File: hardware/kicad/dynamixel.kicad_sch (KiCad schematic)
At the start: 0 parts

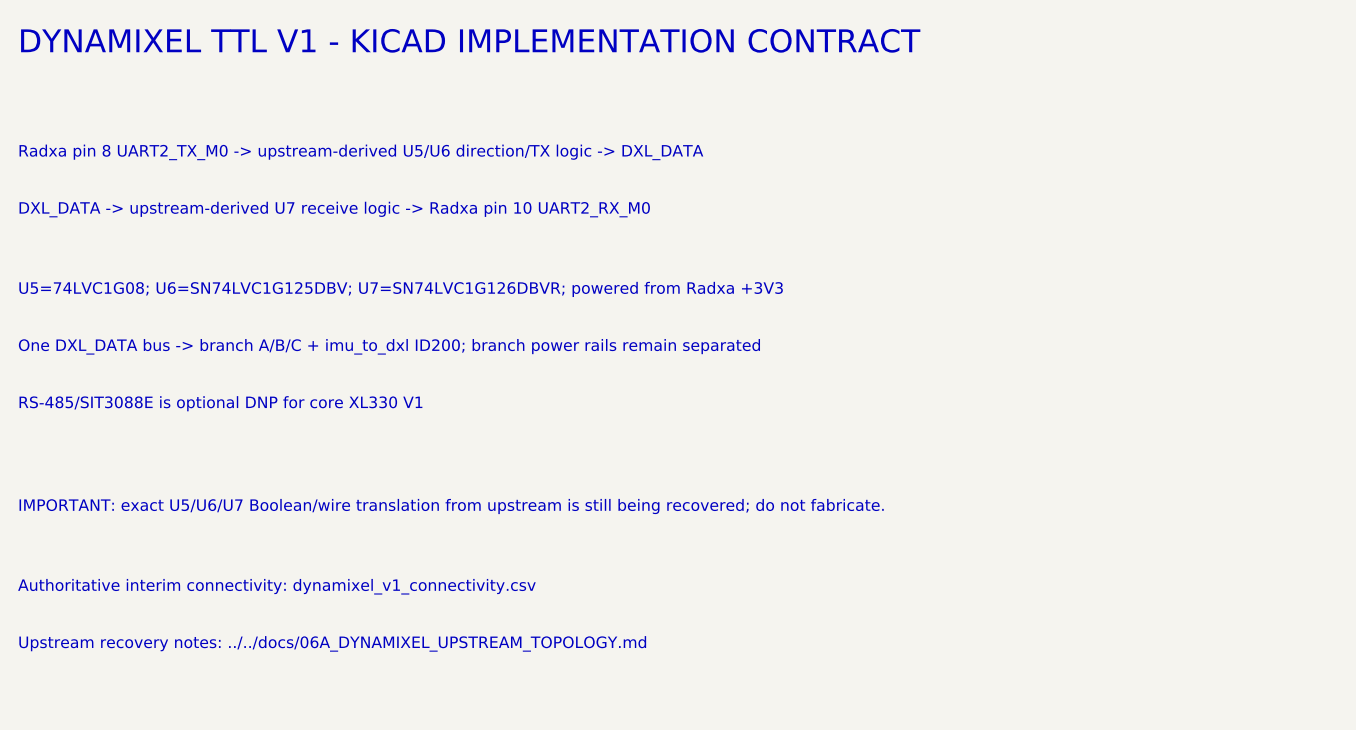
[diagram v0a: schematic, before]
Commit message: correct Dynamixel schematic contract TX RX roles
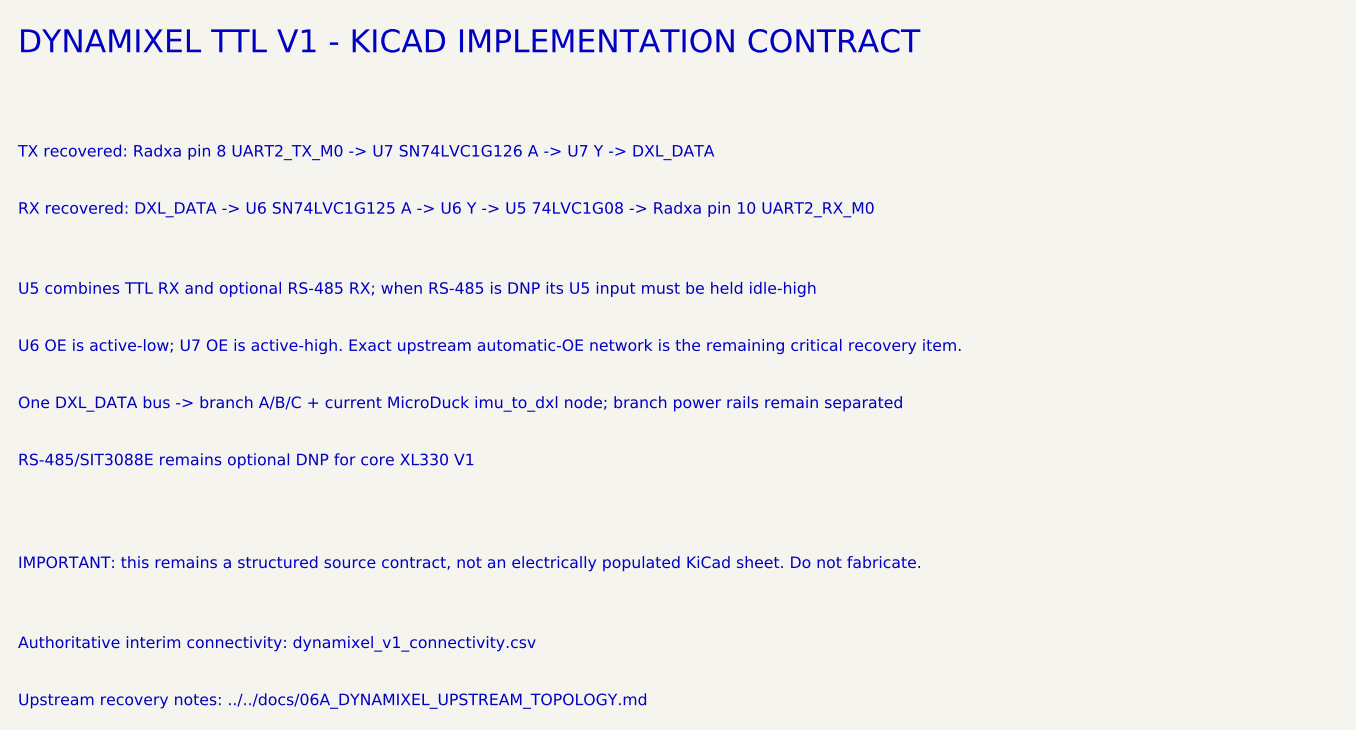
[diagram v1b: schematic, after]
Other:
- note added: "IMPORTANT: this remains a structured source contract, not an electrically populated KiCad sheet. Do not fabricate."
- note added: "One DXL_DATA bus -> branch A/B/C + current MicroDuck imu_to_dxl node; branch power rails remain separated"
- note added: "RS-485/SIT3088E remains optional DNP for core XL330 V1"
- note added: "RX recovered: DXL_DATA -> U6 SN74LVC1G125 A -> U6 Y -> U5 74LVC1G08 -> Radxa pin 10 UART2_RX_M0"
- note added: "TX recovered: Radxa pin 8 UART2_TX_M0 -> U7 SN74LVC1G126 A -> U7 Y -> DXL_DATA"
- note added: "U5 combines TTL RX and optional RS-485 RX; when RS-485 is DNP its U5 input must be held idle-high"
- note added: "U6 OE is active-low; U7 OE is active-high. Exact upstream automatic-OE network is the remaining critical recovery item."
- note removed: "DXL_DATA -> upstream-derived U7 receive logic -> Radxa pin 10 UART2_RX_M0"
- note removed: "IMPORTANT: exact U5/U6/U7 Boolean/wire translation from upstream is still being recovered; do not fabricate."
- note removed: "One DXL_DATA bus -> branch A/B/C + imu_to_dxl ID200; branch power rails remain separated"
- note removed: "RS-485/SIT3088E is optional DNP for core XL330 V1"
- note removed: "Radxa pin 8 UART2_TX_M0 -> upstream-derived U5/U6 direction/TX logic -> DXL_DATA"
- note removed: "U5=74LVC1G08; U6=SN74LVC1G125DBV; U7=SN74LVC1G126DBVR; powered from Radxa +3V3"
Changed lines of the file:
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@@
     (title "Radxa ZERO 3W Robot HAT - Dynamixel TTL V1")
     (date "2026-09-09")
-    (rev "v0.8-dev")
+    (rev "v0.9-dev")
     (company "juper007 / DIY")
     (comment 1 "DESIGN DRAFT - NOT FABRICATION READY")
@@
     (effects (font (size 2.54 2.54) (thickness 0.4)) (justify left bottom))
   )
-  (text "Radxa pin 8 UART2_TX_M0 -> upstream-derived U5/U6 direction/TX logic -> DXL_DATA"
+  (text "TX recovered: Radxa pin 8 UART2_TX_M0 -> U7 SN74LVC1G126 A -> U7 Y -> DXL_DATA"
     (exclude_from_sim no)
     (at 20.32 31.75 0)
     (effects (font (size 1.27 1.27)) (justify left bottom))
   )
-  (text "DXL_DATA -> upstream-derived U7 receive logic -> Radxa pin 10 UART2_RX_M0"
+  (text "RX recovered: DXL_DATA -> U6 SN74LVC1G125 A -> U6 Y -> U5 74LVC1G08 -> Radxa pin 10 UART2_RX_M0"
     (exclude_from_sim no)
     (at 20.32 38.1 0)
     (effects (font (size 1.27 1.27)) (justify left bottom))
   )
-  (text "U5=74LVC1G08; U6=SN74LVC1G125DBV; U7=SN74LVC1G126DBVR; powered from Radxa +3V3"
+  (text "U5 combines TTL RX and optional RS-485 RX; when RS-485 is DNP its U5 input must be held idle-high"
     (exclude_from_sim no)
     (at 20.32 47.0 0)
     (effects (font (size 1.27 1.27)) (justify left bottom))
   )
-  (text "One DXL_DATA bus -> branch A/B/C + imu_to_dxl ID200; branch power rails remain separated"
+  (text "U6 OE is active-low; U7 OE is active-high. Exact upstream automatic-OE network is the remaining critical recovery item."
     (exclude_from_sim no)
     (at 20.32 53.35 0)
     (effects (font (size 1.27 1.27)) (justify left bottom))
   )
-  (text "RS-485/SIT3088E is optional DNP for core XL330 V1"
+  (text "One DXL_DATA bus -> branch A/B/C + current MicroDuck imu_to_dxl node; branch power rails remain separated"
     (exclude_from_sim no)
     (at 20.32 59.7 0)
     (effects (font (size 1.27 1.27)) (justify left bottom))
   )
-  (text "IMPORTANT: exact U5/U6/U7 Boolean/wire translation from upstream is still being recovered; do not fabricate."
+  (text "RS-485/SIT3088E remains optional DNP for core XL330 V1"
     (exclude_from_sim no)
-    (at 20.32 71.12 0)
+    (at 20.32 66.05 0)
+    (effects (font (size 1.27 1.27)) (justify left bottom))
+  )
+  (text "IMPORTANT: this remains a structured source contract, not an electrically populated KiCad sheet. Do not fabricate."
+    (exclude_from_sim no)
+    (at 20.32 77.47 0)
     (effects (font (size 1.27 1.27) (thickness 0.25)) (justify left bottom))
   )
   (text "Authoritative interim connectivity: dynamixel_v1_connectivity.csv"
     (exclude_from_sim no)
-    (at 20.32 80.01 0)
+    (at 20.32 86.36 0)
     (effects (font (size 1.27 1.27)) (justify left bottom))
   )
   (text "Upstream recovery notes: ../../docs/06A_DYNAMIXEL_UPSTREAM_TOPOLOGY.md"
     (exclude_from_sim no)
-    (at 20.32 86.36 0)
+    (at 20.32 92.71 0)
     (effects (font (size 1.27 1.27)) (justify left bottom))
   )

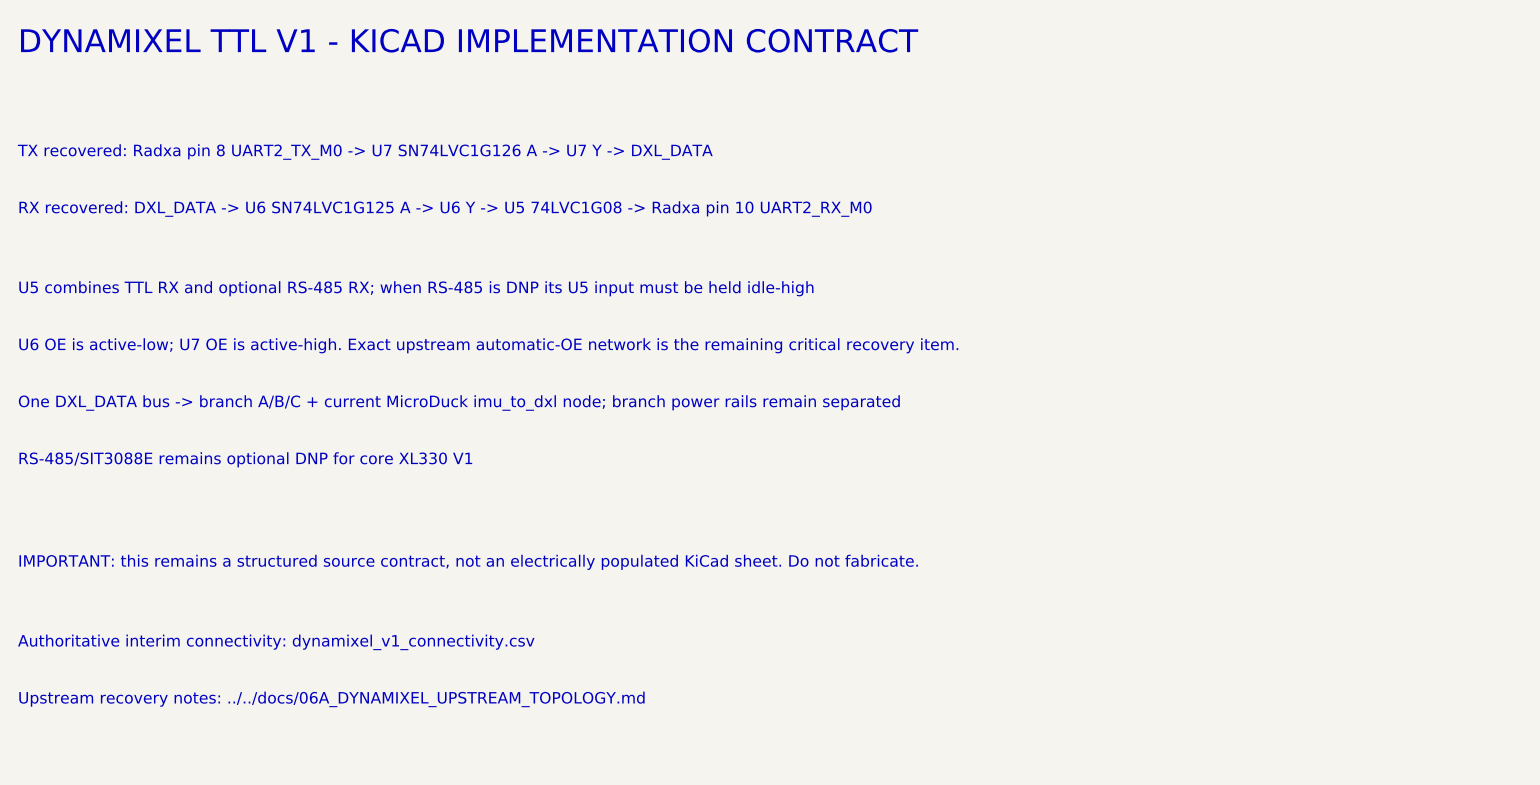
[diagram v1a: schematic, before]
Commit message: synchronize Dynamixel KiCad implementation contract with recovered topology
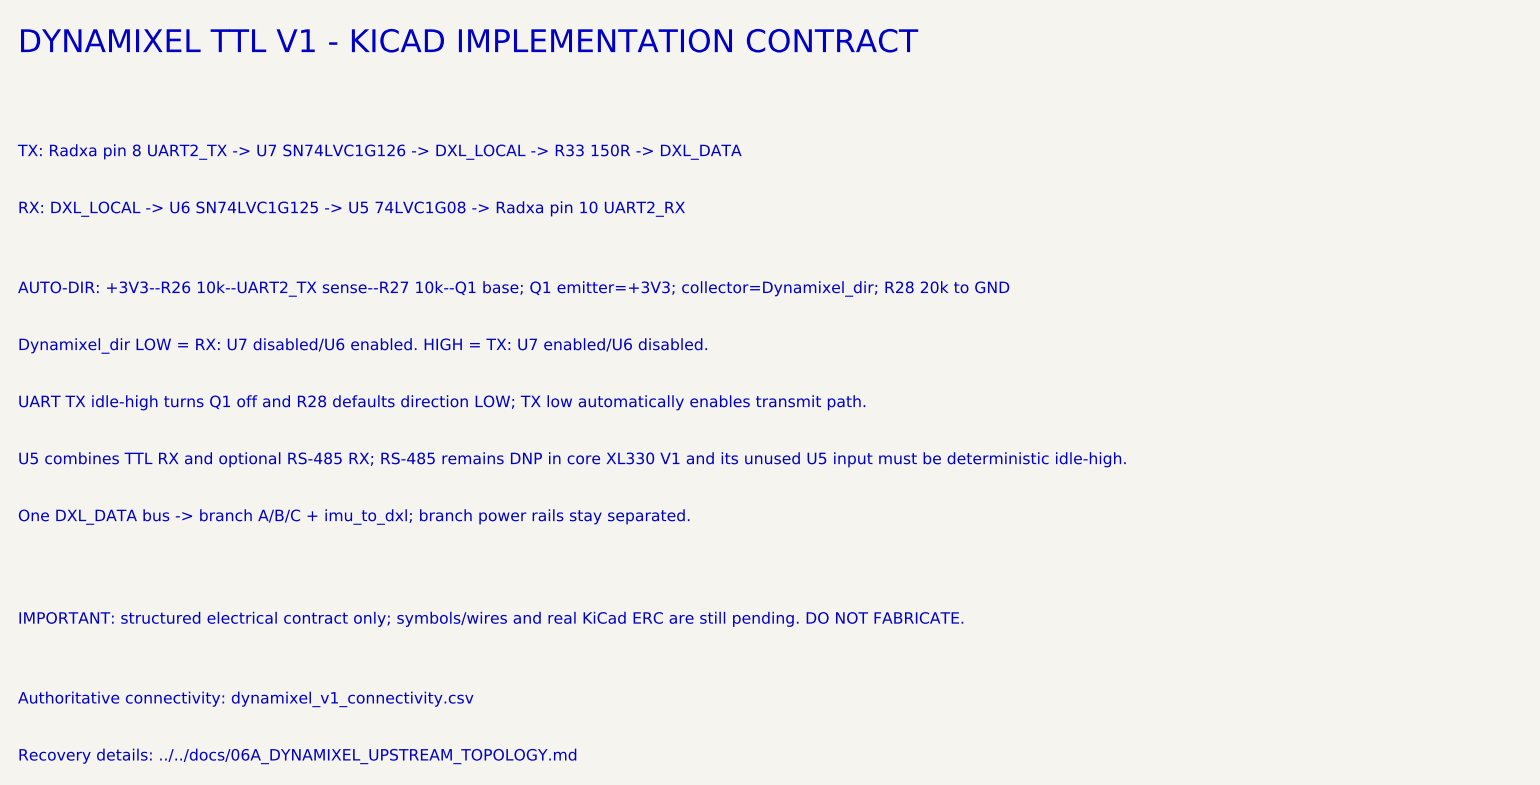
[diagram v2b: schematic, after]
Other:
- note added: "AUTO-DIR: +3V3--R26 10k--UART2_TX sense--R27 10k--Q1 base; Q1 emitter=+3V3; collector=Dynamixel_dir; R28 20k to GND"
- note added: "Authoritative connectivity: dynamixel_v1_connectivity.csv"
- note added: "Dynamixel_dir LOW = RX: U7 disabled/U6 enabled. HIGH = TX: U7 enabled/U6 disabled."
- note added: "IMPORTANT: structured electrical contract only; symbols/wires and real KiCad ERC are still pending. DO NOT FABRICATE."
- note added: "One DXL_DATA bus -> branch A/B/C + imu_to_dxl; branch power rails stay separated."
- note added: "RX: DXL_LOCAL -> U6 SN74LVC1G125 -> U5 74LVC1G08 -> Radxa pin 10 UART2_RX"
- note added: "Recovery details: ../../docs/06A_DYNAMIXEL_UPSTREAM_TOPOLOGY.md"
- note added: "TX: Radxa pin 8 UART2_TX -> U7 SN74LVC1G126 -> DXL_LOCAL -> R33 150R -> DXL_DATA"
- note added: "U5 combines TTL RX and optional RS-485 RX; RS-485 remains DNP in core XL330 V1 and its unused U5 input must be deterministic idle-high."
- note added: "UART TX idle-high turns Q1 off and R28 defaults direction LOW; TX low automatically enables transmit path."
- note removed: "Authoritative interim connectivity: dynamixel_v1_connectivity.csv"
- note removed: "IMPORTANT: this remains a structured source contract, not an electrically populated KiCad sheet. Do not fabricate."
- note removed: "One DXL_DATA bus -> branch A/B/C + current MicroDuck imu_to_dxl node; branch power rails remain separated"
- note removed: "RS-485/SIT3088E remains optional DNP for core XL330 V1"
- note removed: "RX recovered: DXL_DATA -> U6 SN74LVC1G125 A -> U6 Y -> U5 74LVC1G08 -> Radxa pin 10 UART2_RX_M0"
- note removed: "TX recovered: Radxa pin 8 UART2_TX_M0 -> U7 SN74LVC1G126 A -> U7 Y -> DXL_DATA"
- note removed: "U5 combines TTL RX and optional RS-485 RX; when RS-485 is DNP its U5 input must be held idle-high"
- note removed: "U6 OE is active-low; U7 OE is active-high. Exact upstream automatic-OE network is the remaining critical recovery item."
- note removed: "Upstream recovery notes: ../../docs/06A_DYNAMIXEL_UPSTREAM_TOPOLOGY.md"
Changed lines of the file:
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@@
     (title "Radxa ZERO 3W Robot HAT - Dynamixel TTL V1")
     (date "2026-09-09")
-    (rev "v0.9-dev")
+    (rev "v0.12-dev")
     (company "juper007 / DIY")
     (comment 1 "DESIGN DRAFT - NOT FABRICATION READY")
@@
     (effects (font (size 2.54 2.54) (thickness 0.4)) (justify left bottom))
   )
-  (text "TX recovered: Radxa pin 8 UART2_TX_M0 -> U7 SN74LVC1G126 A -> U7 Y -> DXL_DATA"
+  (text "TX: Radxa pin 8 UART2_TX -> U7 SN74LVC1G126 -> DXL_LOCAL -> R33 150R -> DXL_DATA"
     (exclude_from_sim no)
     (at 20.32 31.75 0)
     (effects (font (size 1.27 1.27)) (justify left bottom))
   )
-  (text "RX recovered: DXL_DATA -> U6 SN74LVC1G125 A -> U6 Y -> U5 74LVC1G08 -> Radxa pin 10 UART2_RX_M0"
+  (text "RX: DXL_LOCAL -> U6 SN74LVC1G125 -> U5 74LVC1G08 -> Radxa pin 10 UART2_RX"
     (exclude_from_sim no)
     (at 20.32 38.1 0)
     (effects (font (size 1.27 1.27)) (justify left bottom))
   )
-  (text "U5 combines TTL RX and optional RS-485 RX; when RS-485 is DNP its U5 input must be held idle-high"
+  (text "AUTO-DIR: +3V3--R26 10k--UART2_TX sense--R27 10k--Q1 base; Q1 emitter=+3V3; collector=Dynamixel_dir; R28 20k to GND"
     (exclude_from_sim no)
     (at 20.32 47.0 0)
     (effects (font (size 1.27 1.27)) (justify left bottom))
   )
-  (text "U6 OE is active-low; U7 OE is active-high. Exact upstream automatic-OE network is the remaining critical recovery item."
+  (text "Dynamixel_dir LOW = RX: U7 disabled/U6 enabled. HIGH = TX: U7 enabled/U6 disabled."
     (exclude_from_sim no)
     (at 20.32 53.35 0)
     (effects (font (size 1.27 1.27)) (justify left bottom))
   )
-  (text "One DXL_DATA bus -> branch A/B/C + current MicroDuck imu_to_dxl node; branch power rails remain separated"
+  (text "UART TX idle-high turns Q1 off and R28 defaults direction LOW; TX low automatically enables transmit path."
     (exclude_from_sim no)
     (at 20.32 59.7 0)
     (effects (font (size 1.27 1.27)) (justify left bottom))
   )
-  (text "RS-485/SIT3088E remains optional DNP for core XL330 V1"
+  (text "U5 combines TTL RX and optional RS-485 RX; RS-485 remains DNP in core XL330 V1 and its unused U5 input must be deterministic idle-high."
     (exclude_from_sim no)
     (at 20.32 66.05 0)
     (effects (font (size 1.27 1.27)) (justify left bottom))
   )
-  (text "IMPORTANT: this remains a structured source contract, not an electrically populated KiCad sheet. Do not fabricate."
+  (text "One DXL_DATA bus -> branch A/B/C + imu_to_dxl; branch power rails stay separated."
     (exclude_from_sim no)
-    (at 20.32 77.47 0)
+    (at 20.32 72.4 0)
+    (effects (font (size 1.27 1.27)) (justify left bottom))
+  )
+  (text "IMPORTANT: structured electrical contract only; symbols/wires and real KiCad ERC are still pending. DO NOT FABRICATE."
+    (exclude_from_sim no)
+    (at 20.32 83.82 0)
     (effects (font (size 1.27 1.27) (thickness 0.25)) (justify left bottom))
   )
-  (text "Authoritative interim connectivity: dynamixel_v1_connectivity.csv"
-    (exclude_from_sim no)
-    (at 20.32 86.36 0)
-    (effects (font (size 1.27 1.27)) (justify left bottom))
-  )
-  (text "Upstream recovery notes: ../../docs/06A_DYNAMIXEL_UPSTREAM_TOPOLOGY.md"
+  (text "Authoritative connectivity: dynamixel_v1_connectivity.csv"
     (exclude_from_sim no)
     (at 20.32 92.71 0)
     (effects (font (size 1.27 1.27)) (justify left bottom))
   )
+  (text "Recovery details: ../../docs/06A_DYNAMIXEL_UPSTREAM_TOPOLOGY.md"
+    (exclude_from_sim no)
+    (at 20.32 99.06 0)
+    (effects (font (size 1.27 1.27)) (justify left bottom))
+  )
